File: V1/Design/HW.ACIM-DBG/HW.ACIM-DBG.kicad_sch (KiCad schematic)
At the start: 11 parts

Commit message: V1 layout update 10
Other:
- added sheet PIM (PIM.kicad_sch)
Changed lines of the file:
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@@
+	)
+	(sheet
+		(at 171.45 40.64)
+		(size 19.05 22.86)
+		(fields_autoplaced yes)
+		(stroke
+			(width 0.1524)
+			(type solid)
+		)
+		(fill
+			(color 241 255 177 1.0000)
+		)
+		(property "Sheetname" "PIM"
+			(at 171.45 39.9284 0)
+			(effects
+				(font
+					(size 1.27 1.27)
+				)
+				(justify left bottom)
+			)
+		)
+		(property "Sheetfile" "PIM.kicad_sch"
+			(at 171.45 64.0846 0)
+			(effects
+				(font
+					(size 1.27 1.27)
+				)
+				(justify left top)
+			)
+		)
+		(instances
+			(project "HW.ACIM-DBG"
+				(path "/20f80521-75f2-4ccc-bb34-c9566e70ef5c"
+					(page "5")
+				)
+			)
+		)
 	)
 	(sheet

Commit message: V1 layout update 11
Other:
- sheet TERMINALS ports: added USB_MC_N, USB_MC_P, USB_MC_VBUS, USB_RP_N, USB_RP_P, USB_RP_VBUS; removed USB1_DM, USB1_DP, USB1_VBUS, USB2_DM, USB2_DP, USB2_VBUS

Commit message: V1 layout update 13
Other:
- sheet PIM renamed PIM-PIC32MK
- added sheet PIM-SAME70 (PIM-SAME70.kicad_sch)
- sheet PIM-PIC32MK: file PIM.kicad_sch -> PIM-PIC32MK.kicad_sch
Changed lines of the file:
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@@
+	)
+	(sheet
+		(at 203.2 40.64)
+		(size 26.67 22.86)
+		(fields_autoplaced yes)
+		(stroke
+			(width 0.1524)
+			(type solid)
+		)
+		(fill
+			(color 241 255 177 1.0000)
+		)
+		(property "Sheetname" "PIM-SAME70"
+			(at 203.2 39.9284 0)
+			(effects
+				(font
+					(size 1.27 1.27)
+				)
+				(justify left bottom)
+			)
+		)
+		(property "Sheetfile" "PIM-SAME70.kicad_sch"
+			(at 203.2 64.0846 0)
+			(effects
+				(font
+					(size 1.27 1.27)
+				)
+				(justify left top)
+			)
+		)
+		(instances
+			(project "HW.ACIM-DBG"
+				(path "/20f80521-75f2-4ccc-bb34-c9566e70ef5c"
+					(page "6")
+				)
+			)
+		)
 	)
 	(sheet
@@
 	(sheet
 		(at 171.45 40.64)
-		(size 19.05 22.86)
+		(size 26.67 22.86)
 		(fields_autoplaced yes)
 		(stroke
@@
 			(color 241 255 177 1.0000)
 		)
-		(property "Sheetname" "PIM"
+		(property "Sheetname" "PIM-PIC32MK"
 			(at 171.45 39.9284 0)
 			(effects
@@
 			)
 		)
-		(property "Sheetfile" "PIM.kicad_sch"
+		(property "Sheetfile" "PIM-PIC32MK.kicad_sch"
 			(at 171.45 64.0846 0)
 			(effects

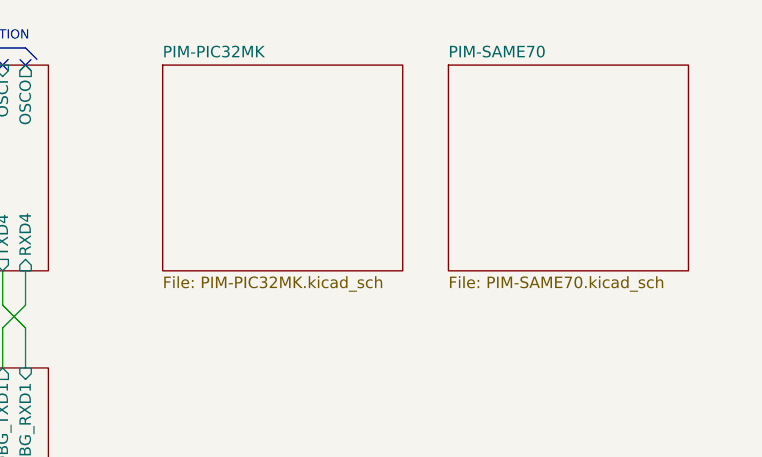
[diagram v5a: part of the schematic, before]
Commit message: Production HW.ACIM-DBG_V1.0 update 3D, USB drivers
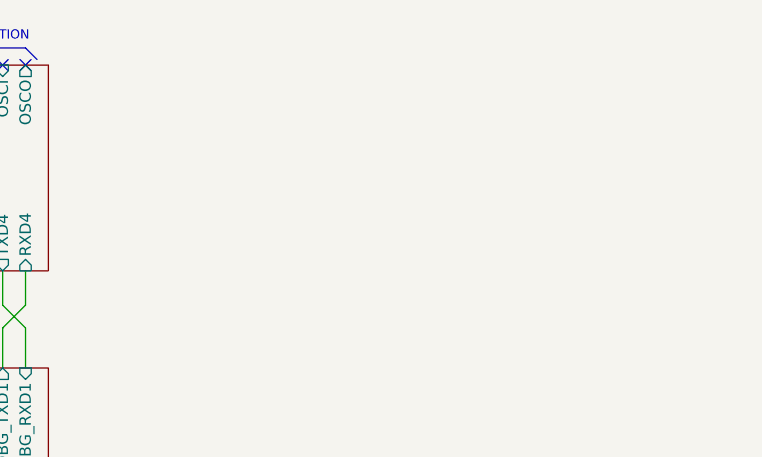
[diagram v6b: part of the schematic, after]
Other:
- removed sheet PIM-PIC32MK
- removed sheet PIM-SAME70
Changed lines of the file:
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@@
-	)
-	(sheet
-		(at 203.2 40.64)
-		(size 26.67 22.86)
-		(exclude_from_sim no)
-		(in_bom yes)
-		(on_board yes)
-		(dnp no)
-		(fields_autoplaced yes)
-		(stroke
-			(width 0.1524)
-			(type solid)
-		)
-		(fill
-			(color 241 255 177 1.0000)
-		)
-		(property "Sheetname" "PIM-SAME70"
-			(at 203.2 39.9284 0)
-			(effects
-				(font
-					(size 1.27 1.27)
-				)
-				(justify left bottom)
-			)
-		)
-		(property "Sheetfile" "PIM-SAME70.kicad_sch"
-			(at 203.2 64.0846 0)
-			(effects
-				(font
-					(size 1.27 1.27)
-				)
-				(justify left top)
-			)
-		)
-		(instances
-			(project "HW.ACIM-DBG"
-				(path "/20f80521-75f2-4ccc-bb34-c9566e70ef5c"
-					(page "6")
-				)
-			)
-		)
 	)
 	(sheet
@@
 				)
 			)
-		)
-	)
-	(sheet
-		(at 171.45 40.64)
-		(size 26.67 22.86)
-		(exclude_from_sim no)
-		(in_bom yes)
-		(on_board yes)
-		(dnp no)
-		(fields_autoplaced yes)
-		(stroke
-			(width 0.1524)
-			(type solid)
-		)
-		(fill
-			(color 241 255 177 1.0000)
-		)
-		(property "Sheetname" "PIM-PIC32MK"
-			(at 171.45 39.9284 0)
-			(effects
-				(font
-					(size 1.27 1.27)
-				)
-				(justify left bottom)
-			)
-		)
-		(property "Sheetfile" "PIM-PIC32MK.kicad_sch"
-			(at 171.45 64.0846 0)
-			(effects
-				(font
-					(size 1.27 1.27)
-				)
-				(justify left top)
-			)
-		)
-		(instances
-			(project "HW.ACIM-DBG"
-				(path "/20f80521-75f2-4ccc-bb34-c9566e70ef5c"
-					(page "5")
-				)
-			)
